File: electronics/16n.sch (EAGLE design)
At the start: 112 parts, among them J1 PJ302M, J10 PJ302M, J11 PJ302M, J12 PJ302M, J13 PJ302M, J14 PJ302M, J15 PJ302M, J16 PJ302M, J2 PJ302M, J3 PJ302M, J4 PJ302M, J5 PJ302M, J6 PJ302M, J7 PJ302M, J8 PJ302M, J9 PJ302M, U1 CD74HC4067SM96, U2 MCP6004_SMD, U3 MCP6004_SMD, U4 MCP6004_SMD, U5 MCP6004_SMD, U6 MCP6004_SMD, U7 MCP6004_SMD, U8 MCP6004_SMD, U9 MCP6004

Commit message: Organize opamp page.  General cleanup.
Move wipers and CV jacks to 2nd page and lay out in a clearer way.  Add frames that work with cross reference symbols.
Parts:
- U$10: SPICEPREFIX (none) -> U
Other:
- moved on the sheet: R1, R10, R11, R12, R13, R14, R15, R16, R19, R2, R20, R21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

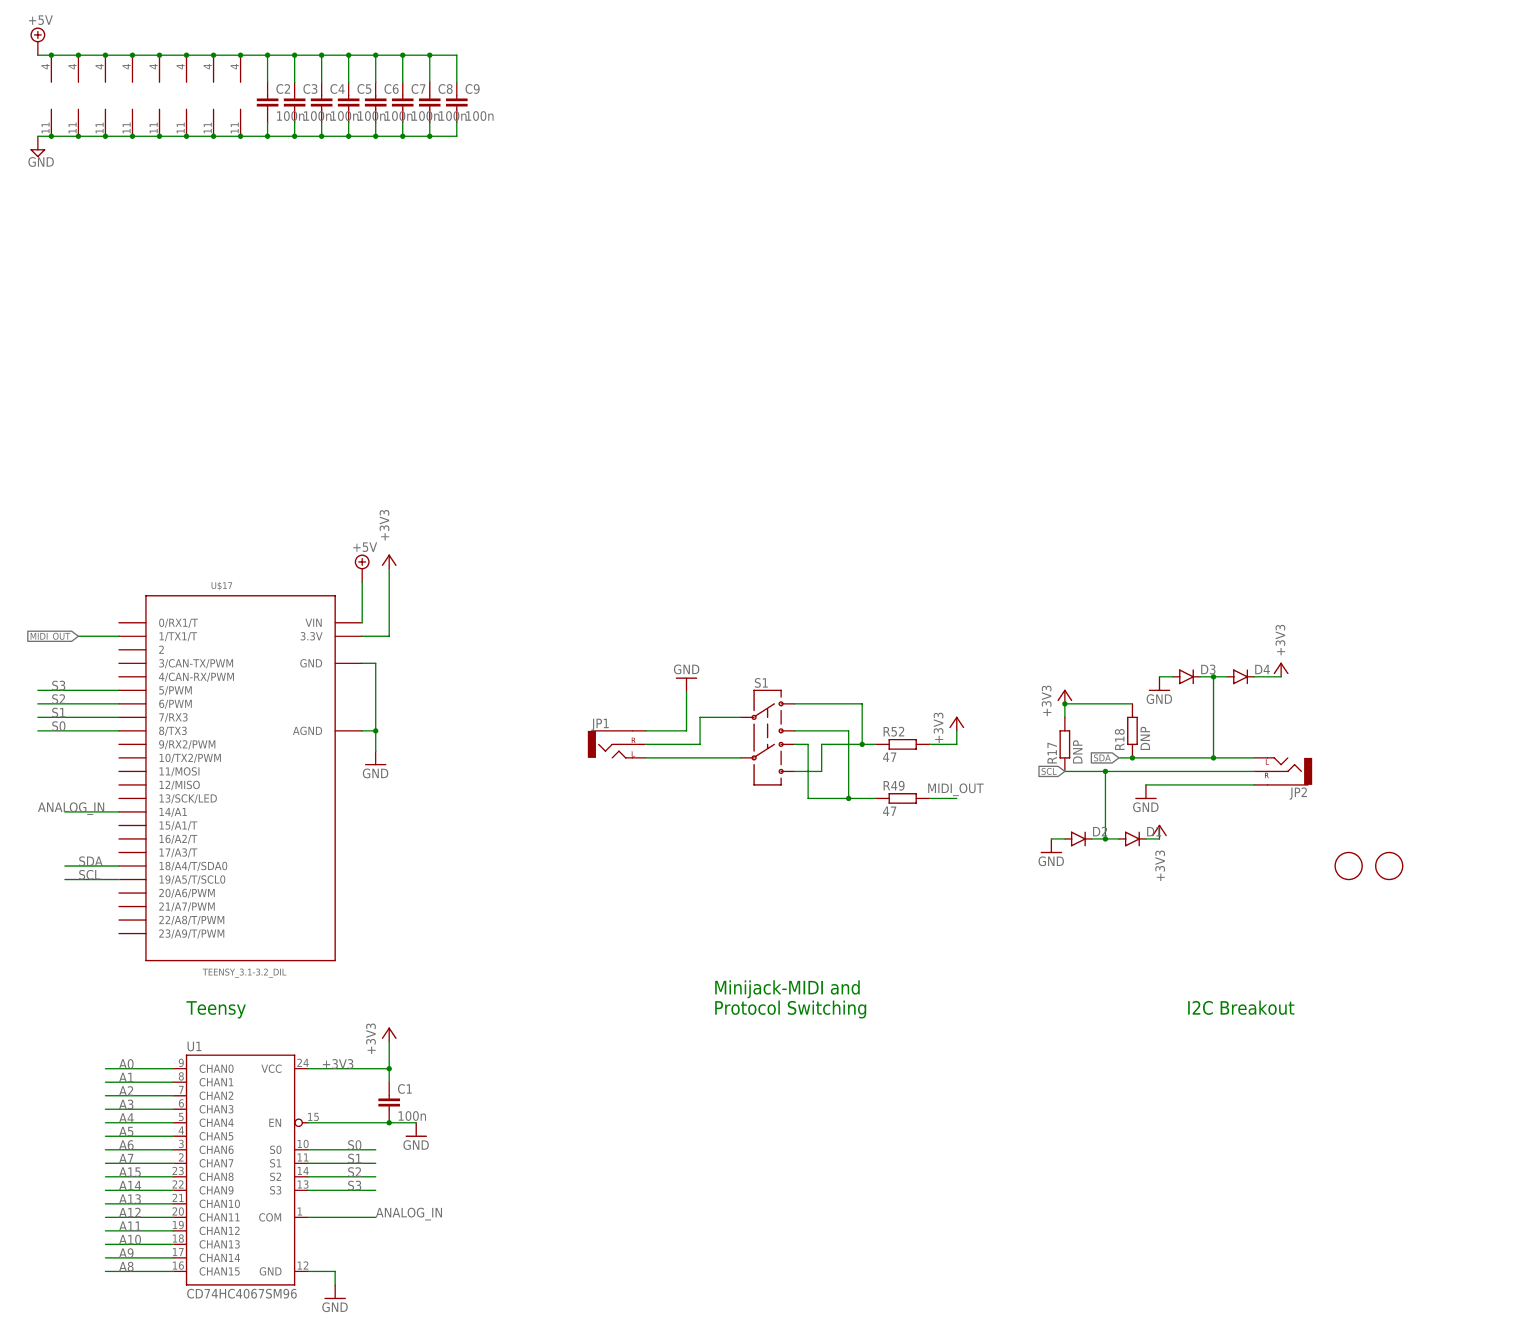
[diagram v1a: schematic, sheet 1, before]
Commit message: Organize first page of schematic
Moved things around, made net labels and supply symbols consistent, add labels
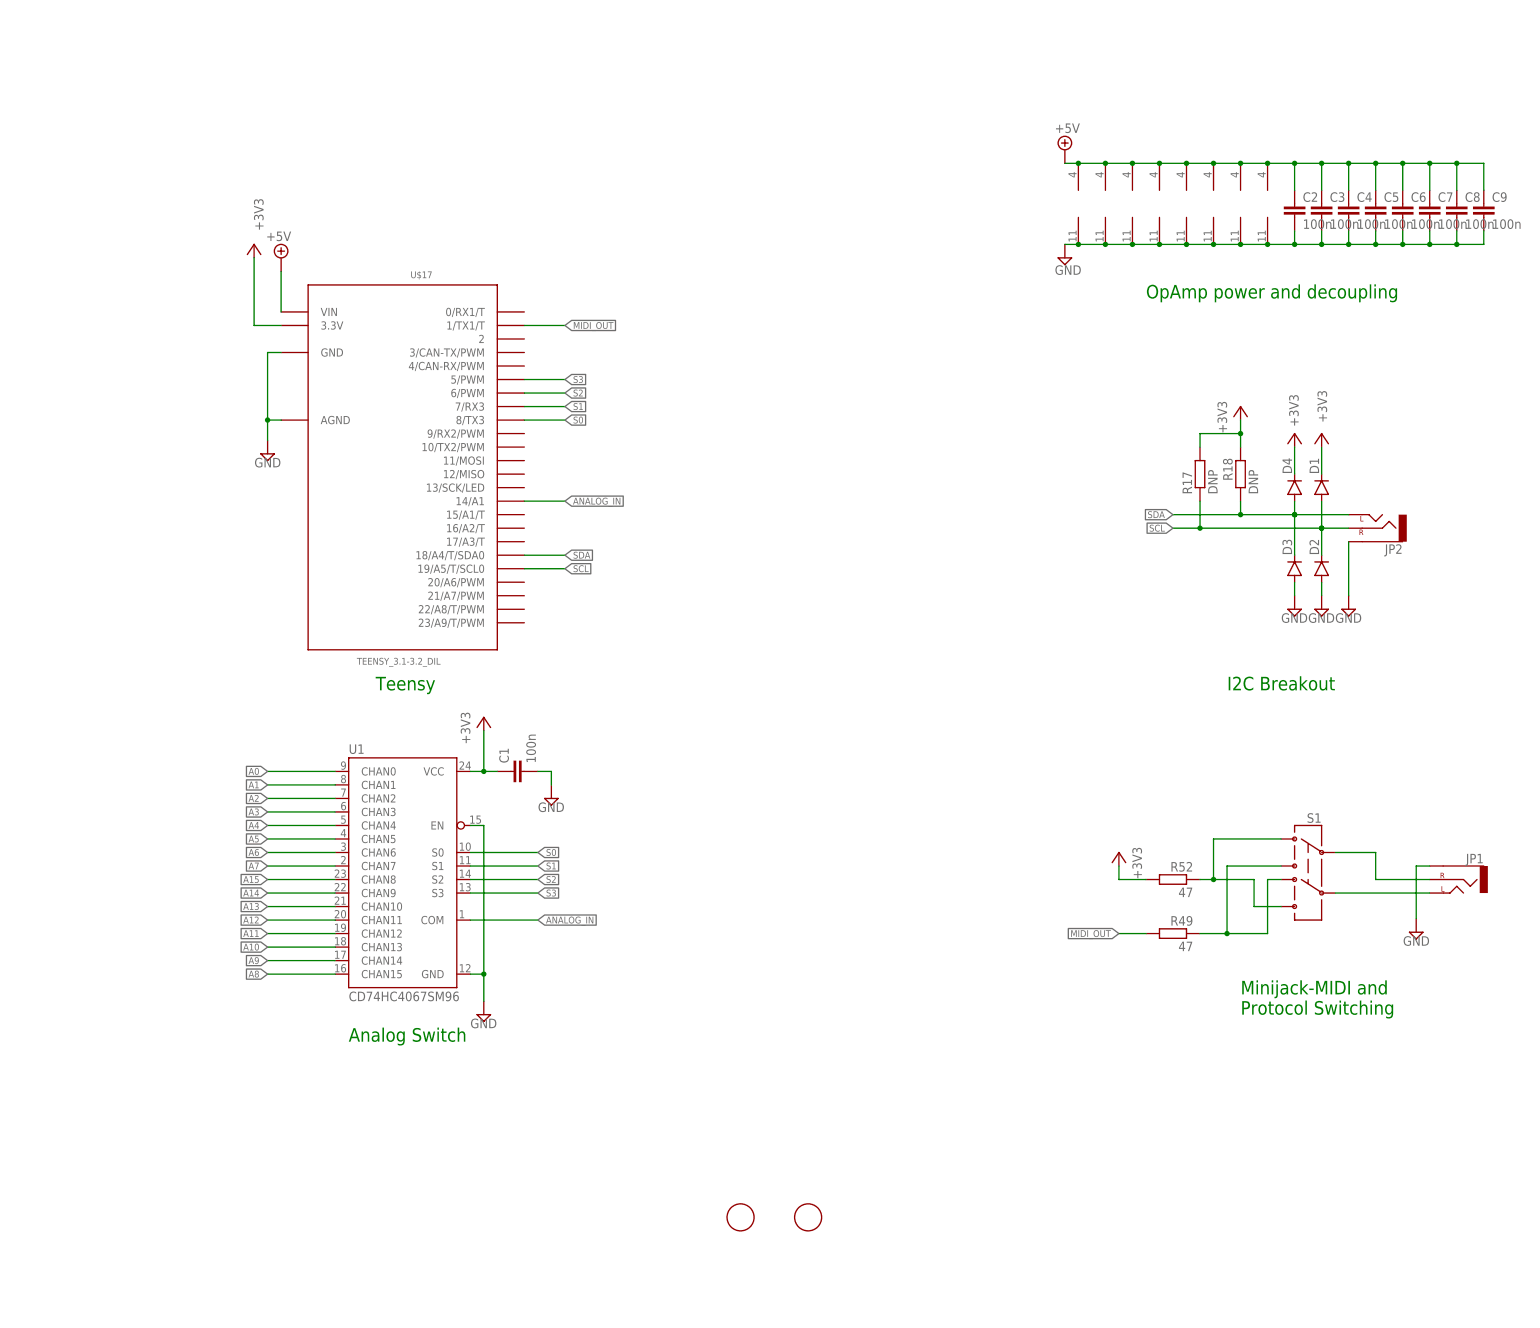
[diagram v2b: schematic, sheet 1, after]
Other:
- note added: "Analog Switch"
- note added: "OpAmp power and decoupling"
- moved on the sheet: C1, C2, C3, C4, C5, C6, C7, C8, C9, D1, D2, D3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
